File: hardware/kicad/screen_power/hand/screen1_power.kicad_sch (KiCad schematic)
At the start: 16 parts, among them J103 EVM 5V, J104 EVM CONTROL, K102 G5LE-1 DC5, Q101 2N7000, Q102 2N3906, Q103 IRLZ44NPBF

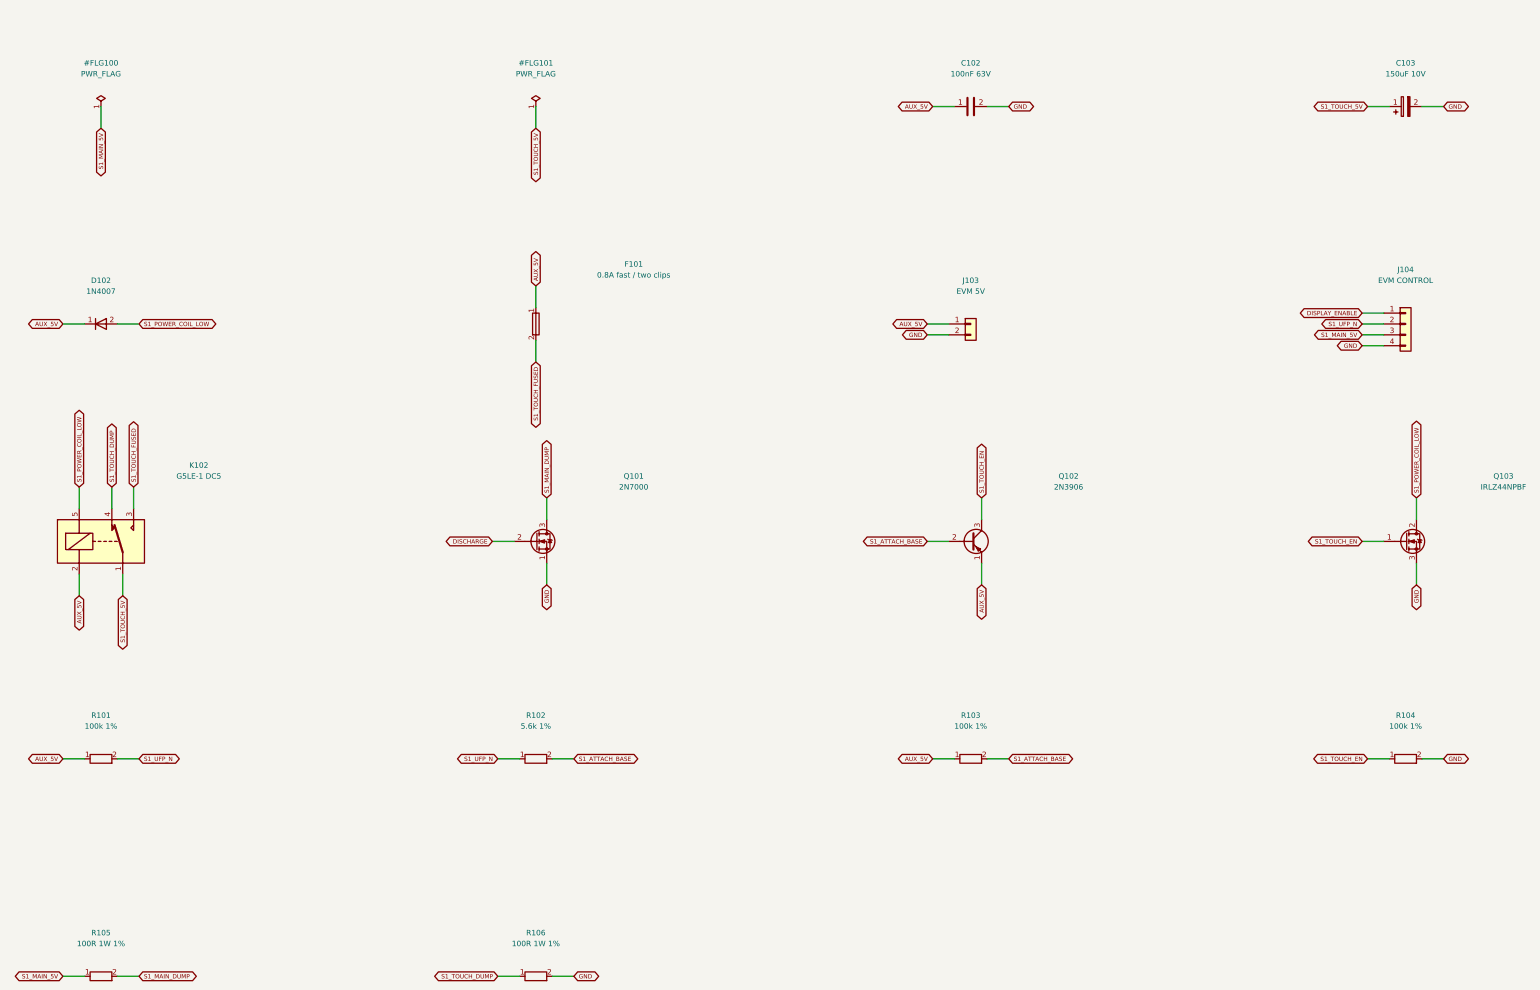
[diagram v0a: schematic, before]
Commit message: refactor(hardware): simplify and compact screen power boards
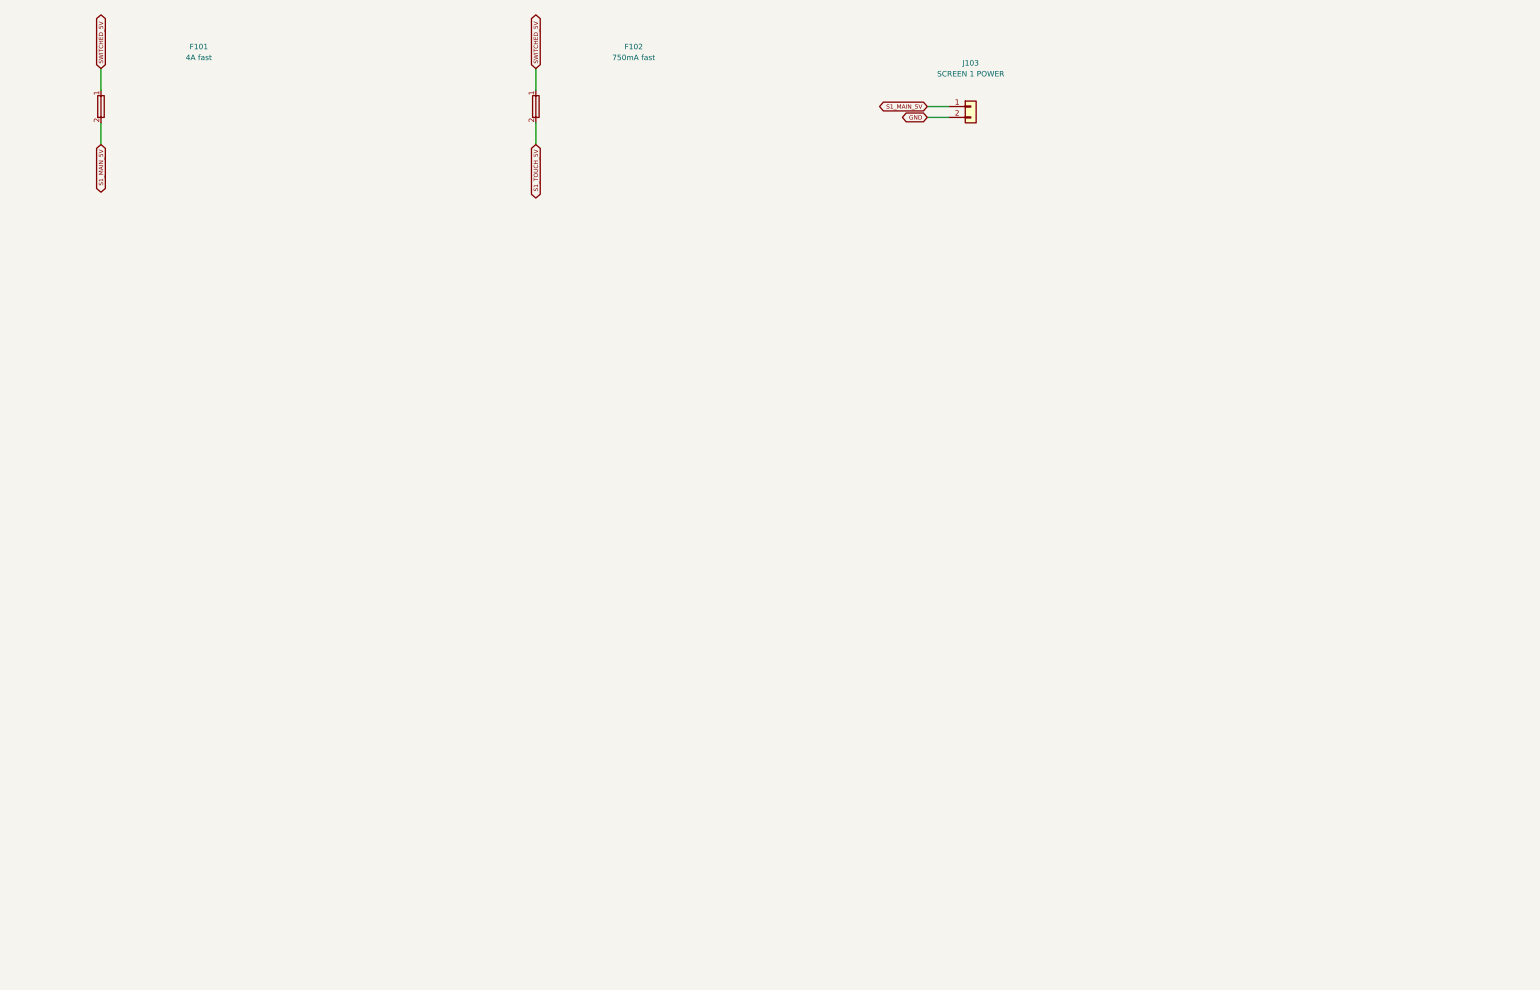
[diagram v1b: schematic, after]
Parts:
- removed C102: 100nF 63V, Capacitor_THT:C_Rect_L7.2mm_W2.5mm_P5.00mm, symbol screen_symbols:Device_C
- removed C103: 150uF 10V, Capacitor_THT:CP_Radial_D5.0mm_P2.00mm, symbol screen_symbols:Device_C_Polarized
- removed D102: 1N4007, Diode_THT:D_DO-41_SOD81_P10.16mm_Horizontal, symbol screen_symbols:Diode_1N4007
- removed J104: EVM CONTROL, Connector_JST:JST_XH_B4B-XH-A_1x04_P2.50mm_Vertical, symbol screen_symbols:Connector_Generic_Conn_01x04
- removed K102: G5LE-1 DC5, Relay_THT:Relay_SPDT_Omron-G5LE-1, symbol screen_symbols:Relay_G5LE-1
- removed Q101: 2N7000, Package_TO_SOT_THT:TO-92_Inline_Wide, symbol screen_symbols:Transistor_FET_2N7000
- removed Q102: 2N3906, Package_TO_SOT_THT:TO-92_Inline_Wide, symbol screen_symbols:Transistor_BJT_2N3906
- removed Q103: IRLZ44NPBF, Package_TO_SOT_THT:TO-220-3_Vertical, symbol screen_symbols:Transistor_FET_IRLZ44N
- removed R101, R103, R104: 100k 1%, Resistor_THT:R_Axial_DIN0207_L6.3mm_D2.5mm_P10.16mm_Horizontal, symbol screen_symbols:Device_R
- removed R102: 5.6k 1%, Resistor_THT:R_Axial_DIN0207_L6.3mm_D2.5mm_P10.16mm_Horizontal, symbol screen_symbols:Device_R
- removed R105, R106: 100R 1W 1%, Resistor_THT:R_Axial_DIN0207_L6.3mm_D2.5mm_P10.16mm_Horizontal, symbol screen_symbols:Device_R
- added F102: 750mA fast, screen_power:Fuse_Littelfuse_251_P12.70mm, symbol screen_symbols:Device_Fuse
- F101: value 0.8A fast / two clips -> 4A fast; footprint Fuse:Fuseholder_Clip-5x20mm_Littelfuse_111_Lateral_P18.80x5.00mm_D1.17mm_Horizontal -> screen_power:Fuse_Littelfuse_251_P12.70mm; MPN 01110501Z -> 0251004.MXL
- J103: value EVM 5V -> SCREEN 1 POWER
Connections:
- net S1_TOUCH_FUSED is gone; now on net S1_MAIN_5V: F101.2
- net S1_MAIN_5V: now also J103.1 (Pin_1)
- net S1_TOUCH_5V: now also F102.2
- net AUX_5V renamed SWITCHED_5V
- net SWITCHED_5V: now also F102.1; no longer J103.1 (Pin_1)
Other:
- moved on the sheet: F101, J103

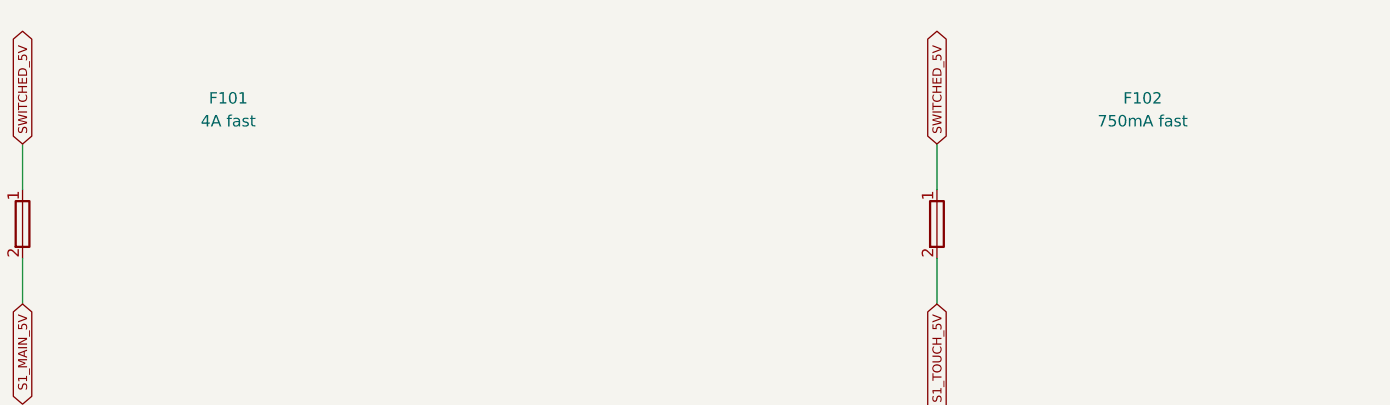
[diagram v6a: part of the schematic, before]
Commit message: feat(hardware): lower screen power cost and finish copper contours
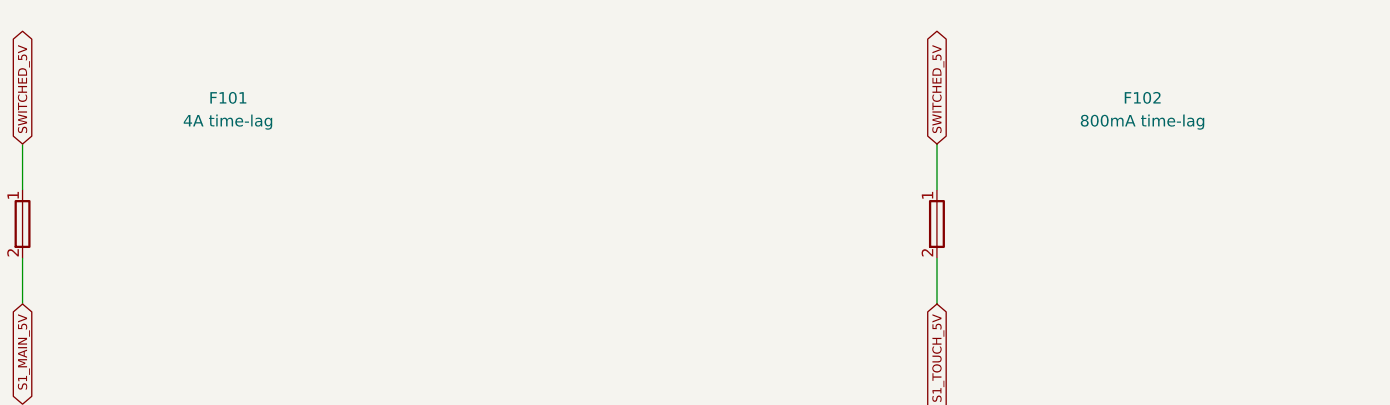
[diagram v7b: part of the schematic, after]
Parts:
- F101: value 4A fast -> 4A time-lag; footprint screen_power:Fuse_Littelfuse_251_P12.70mm -> screen_power:Fuse_Bel_0697H_P5.08mm; MPN 0251004.MXL -> 0697H4000-02
- F102: value 750mA fast -> 800mA time-lag; footprint screen_power:Fuse_Littelfuse_251_P12.70mm -> screen_power:Fuse_Bel_0697H_P5.08mm; MPN 0251.750MXL -> 0697H0800-02
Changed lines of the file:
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@@
   (title_block
     (title "Segno screen power / hand / screen1 power")
-    (rev "M prototype")
-    (comment 1 "AUX-powered relays; each host VBUS supplies only its presence detector.")
-    (comment 2 "Physical verification required before release."))
+    (rev "N prototype")
+    (comment 1 "One normally open contact switches AUX; every board load sits behind F1.")
+    (comment 2 "AUX-powered relays; each host VBUS supplies only its presence detector.")
+    (comment 3 "Physical verification required before release."))
   (wire
     (pts
@@
         (font
           (size 1.27 1.27))))
-    (property "Value" "4A fast"
+    (property "Value" "4A time-lag"
       (at 73.66 52.07 0)
       (effects
         (font
           (size 1.27 1.27))))
-    (property "Footprint" "screen_power:Fuse_Littelfuse_251_P12.70mm"
+    (property "Footprint" "screen_power:Fuse_Bel_0697H_P5.08mm"
       (at 73.66 63.5 0)
       (effects
@@
           (size 1.27 1.27))
         (hide yes)))
-    (property "MPN" "0251004.MXL"
+    (property "MPN" "0697H4000-02"
       (at 73.66 63.5 0)
       (effects
@@
         (font
           (size 1.27 1.27))))
-    (property "Value" "750mA fast"
+    (property "Value" "800mA time-lag"
       (at 175.26 52.07 0)
       (effects
         (font
           (size 1.27 1.27))))
-    (property "Footprint" "screen_power:Fuse_Littelfuse_251_P12.70mm"
+    (property "Footprint" "screen_power:Fuse_Bel_0697H_P5.08mm"
       (at 175.26 63.5 0)
       (effects
@@
           (size 1.27 1.27))
         (hide yes)))
-    (property "MPN" "0251.750MXL"
+    (property "MPN" "0697H0800-02"
       (at 175.26 63.5 0)
       (effects
